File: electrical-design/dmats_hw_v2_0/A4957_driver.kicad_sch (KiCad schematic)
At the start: 21 parts, among them Q1 PSMN1R0-30YLC,115, Q2 PSMN1R0-30YLC,115, Q3 PSMN1R0-30YLC,115, Q4 PSMN1R0-30YLC,115, U1 A4957

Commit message: v2 of circuit for PCB
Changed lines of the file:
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@@
   (symbol (lib_id "Device:R") (at 179.07 99.06 90) (mirror x) (unit 1)
     (in_bom yes) (on_board yes) (dnp no)
-    (property "Reference" "R9" (at 179.07 93.8022 90)
+    (property "Reference" "R9" (at 182.88 95.4786 90)
       (effects (font (size 1.27 1.27)))
     )
-    (property "Value" "1K" (at 179.07 96.1136 90)
+    (property "Value" "1K" (at 182.88 97.79 90)
       (effects (font (size 1.27 1.27)))
     )

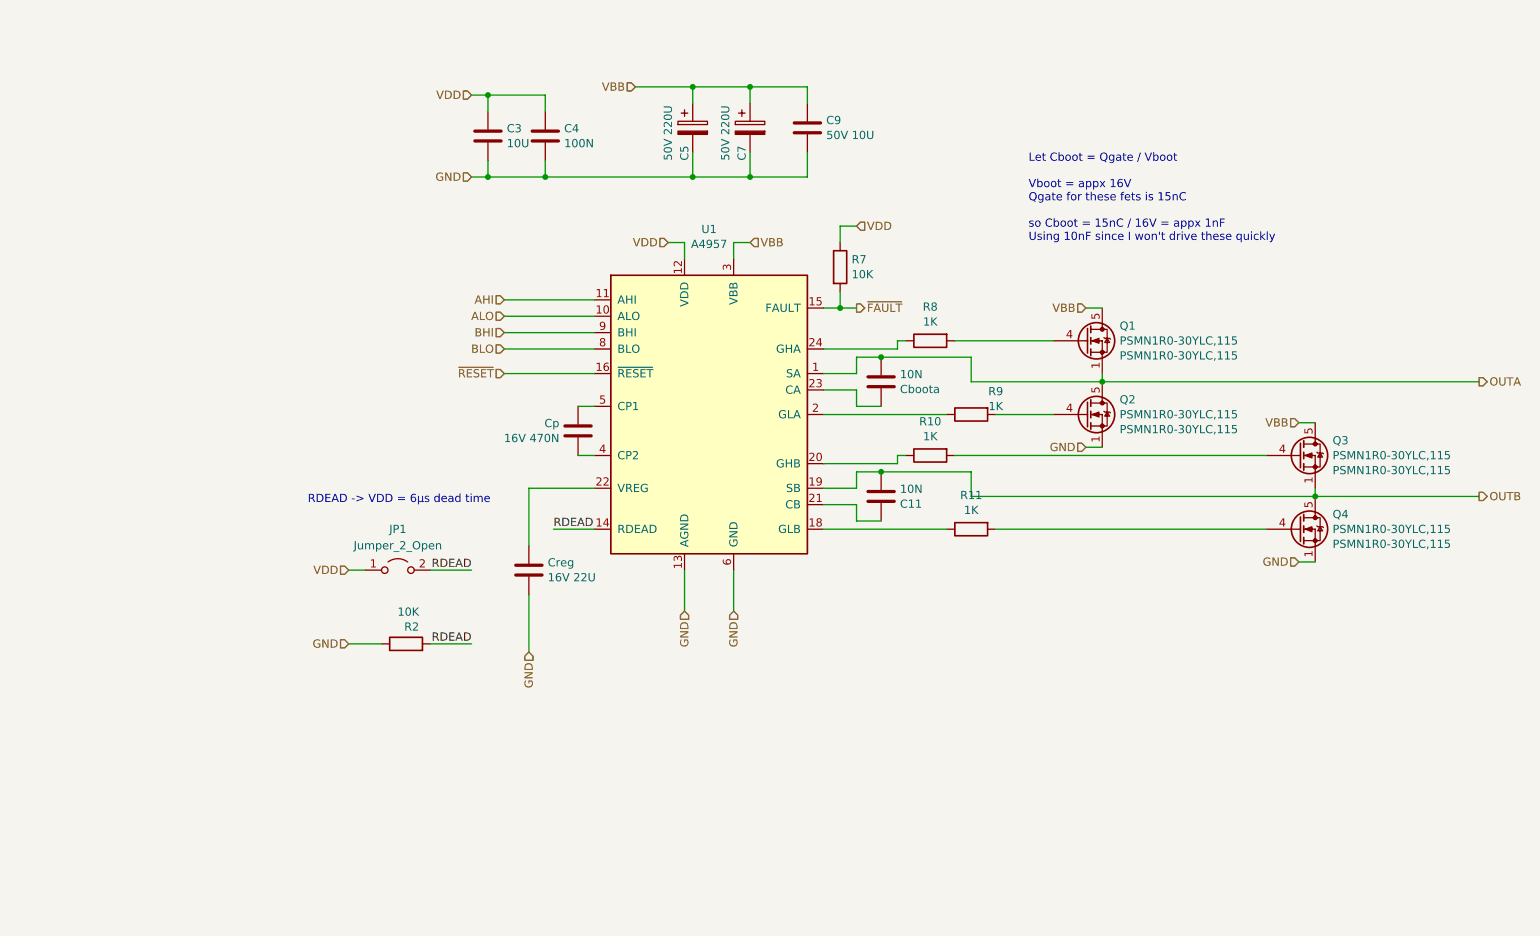
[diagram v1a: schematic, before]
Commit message: created all PCB footprints
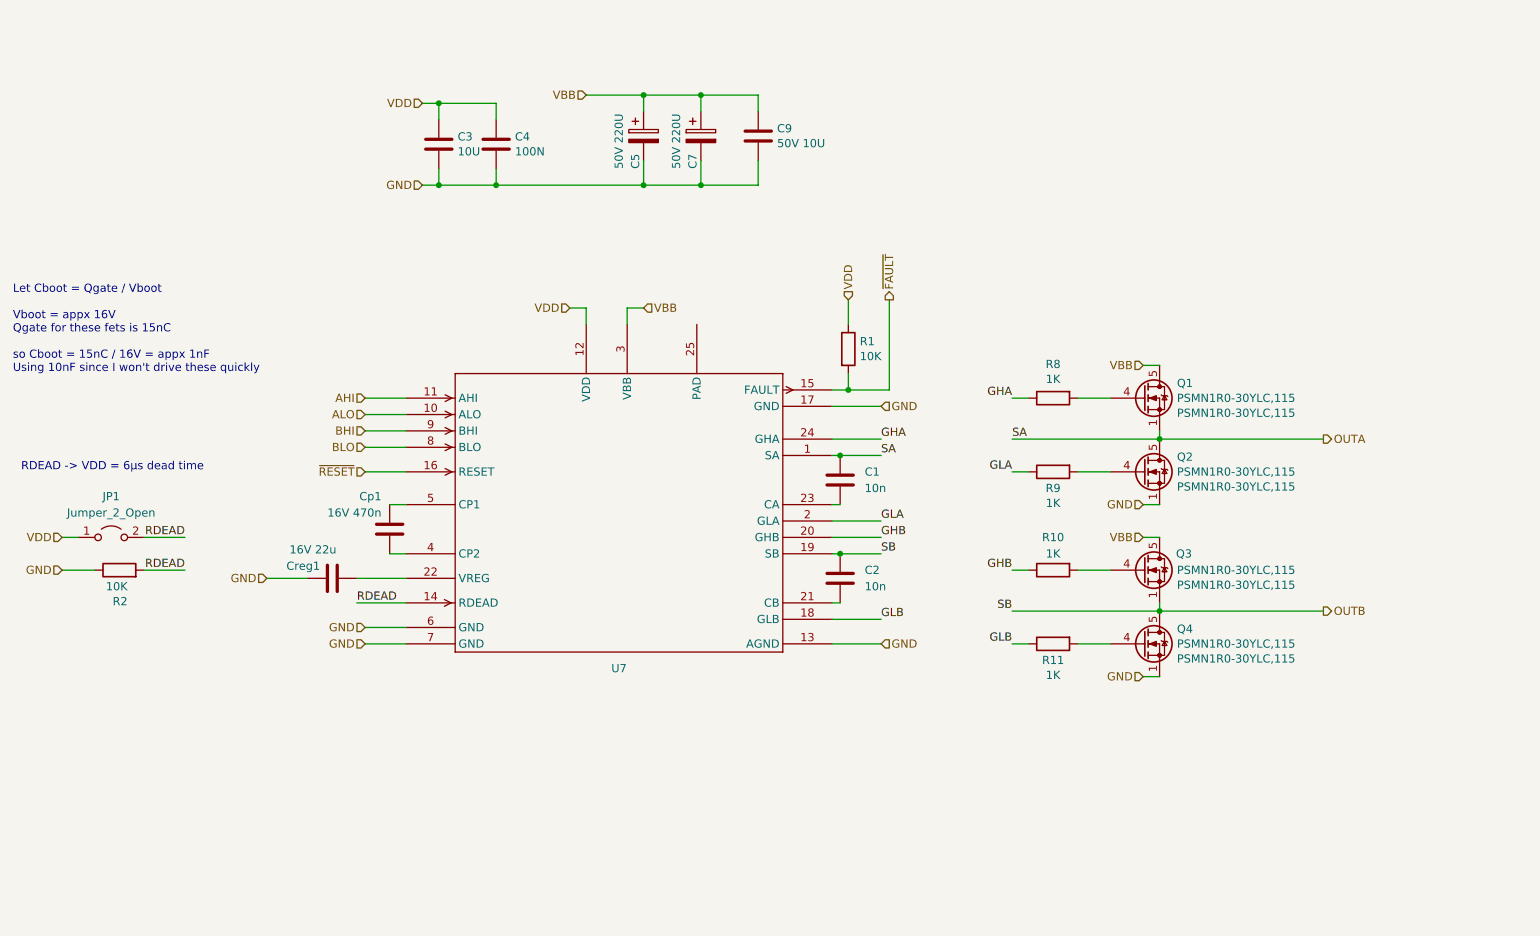
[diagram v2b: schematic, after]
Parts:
- removed C11, Cboota: 10N, Capacitor_SMD:C_0603_1608Metric, symbol Device:C
- removed Cp: 16V 470N, Capacitor_SMD:C_0805_2012Metric, symbol Device:C
- removed Creg: 16V 22U, Capacitor_SMD:C_0805_2012Metric, symbol Device:C
- removed R7: 10K, Resistor_SMD:R_0603_1608Metric, symbol Device:R
- removed U1: A4957, william_motor:A4957, symbol william_motor:A4957
- added C1, C2: 10n, symbol Device:C
- added Cp1: 16V 470n, Capacitor_SMD:C_0805_2012Metric, symbol Device:C
- added Creg1: 16V 22u, Capacitor_SMD:C_0805_2012Metric, symbol Device:C
- added R1: 10K, Resistor_SMD:R_0603_1608Metric, symbol Device:R
- added U7: ~, DMATS_capstone:QFN-24_ALM, symbol DMATS_capstone:A4957
- JP1: footprint (none) -> Resistor_SMD:R_0402_1005Metric_Pad0.72x0.64mm_HandSolder
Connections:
- net AHI: now also U7.11 (AHI)
- net ALO: now also U7.10 (ALO)
- net BHI: now also U7.9 (BHI)
- net BLO: now also U7.8 (BLO)
- net GND: now also Creg1.2, U7.13 (AGND), U7.17 (GND), U7.6 (GND), U7.7 (GND)
- net OUTA: now also C1.1, U7.1 (SA)
- net OUTB: now also C2.1, U7.19 (SB)
- net RDEAD: now also U7.14 (RDEAD)
- net VBB: now also U7.3 (VBB)
- net VDD: now also R1.1, U7.12 (VDD)
- net ~{FAULT}: now also R1.2, U7.15 (FAULT)
- net ~{RESET}: now also U7.16 (RESET)
- net GLA: now reaches R9.1
- net GLA: now also U7.2 (GLA)
- net GHA: now reaches R8.1
- net GHA: now also U7.24 (GHA)
- net GLB: now reaches R11.1
- net GLB: now also U7.18 (GLB)
- net GHB: now reaches R10.1
- net GHB: now also U7.20 (GHB)
- new net: C2.2, U7.21 (CB)
- new net: Cp1.1, U7.4 (CP2)
- new net: Cp1.2, U7.5 (CP1)
- new net: Creg1.1, U7.22 (VREG)
- new net: C1.2, U7.23 (CA)
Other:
- moved on the sheet: C3, C4, C5, C7, C9, JP1, Q1, Q2, Q3, Q4, R10, R11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

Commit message: bulk of PCB design layout complete
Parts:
- C1, C2: footprint (none) -> Capacitor_SMD:C_0603_1608Metric
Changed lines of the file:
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@@
       (effects (font (size 1.27 1.27)) (justify left))
     )
-    (property "Footprint" "" (at 159.7152 128.27 0)
+    (property "Footprint" "Capacitor_SMD:C_0603_1608Metric" (at 159.7152 128.27 0)
       (effects (font (size 1.27 1.27)) hide)
     )
@@
       (effects (font (size 1.27 1.27)) (justify left))
     )
-    (property "Footprint" "" (at 159.7152 113.03 0)
+    (property "Footprint" "Capacitor_SMD:C_0603_1608Metric" (at 159.7152 113.03 0)
       (effects (font (size 1.27 1.27)) hide)
     )

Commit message: PCB work
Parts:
- JP1: footprint Resistor_SMD:R_0402_1005Metric_Pad0.72x0.64mm_HandSolder -> Resistor_SMD:R_0603_1608Metric
- U7: footprint DMATS_capstone:QFN-24_ALM -> Package_DFN_QFN:HVQFN-24-1EP_4x4mm_P0.5mm_EP2.6x2.6mm_ThermalVias
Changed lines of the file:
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@@
       (effects (font (size 1.27 1.27)))
     )
-    (property "Footprint" "Resistor_SMD:R_0402_1005Metric_Pad0.72x0.64mm_HandSolder" (at 45.72 118.11 0)
+    (property "Footprint" "Resistor_SMD:R_0603_1608Metric" (at 45.72 118.11 0)
       (effects (font (size 1.27 1.27)) hide)
     )
@@
       (effects (font (size 1.27 1.27)))
     )
-    (property "Footprint" "DMATS_capstone:QFN-24_ALM" (at 99.06 132.715 0)
+    (property "Footprint" "Package_DFN_QFN:HVQFN-24-1EP_4x4mm_P0.5mm_EP2.6x2.6mm_ThermalVias" (at 99.06 132.715 0)
       (effects (font (size 1.27 1.27)) hide)
     )

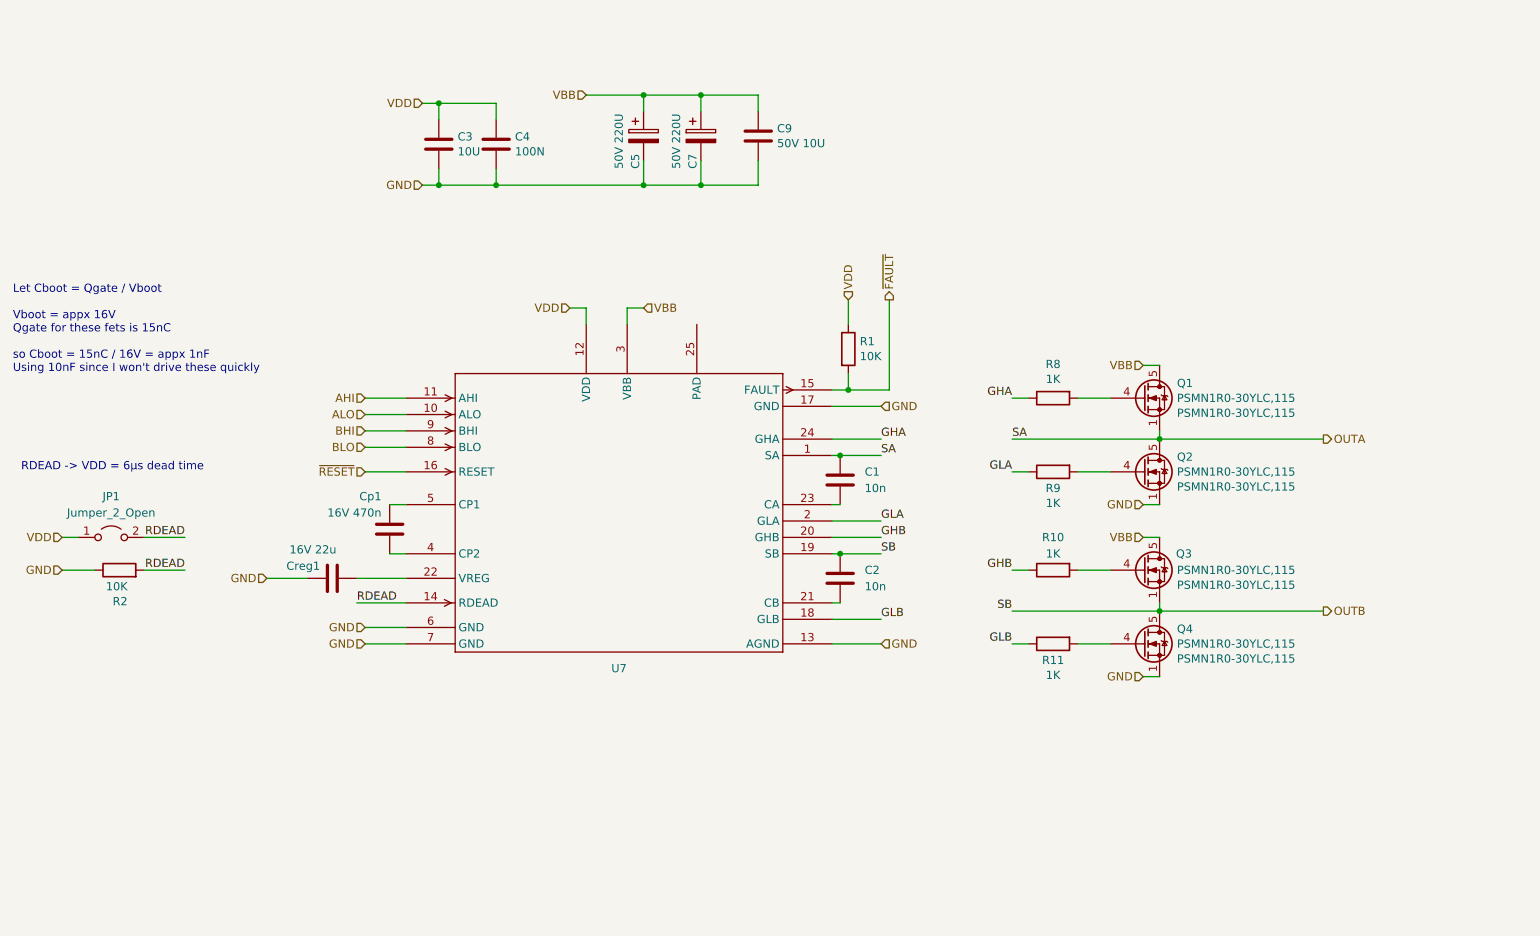
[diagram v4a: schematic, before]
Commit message: sim updates for force analysis and visual clean up on elec drawings
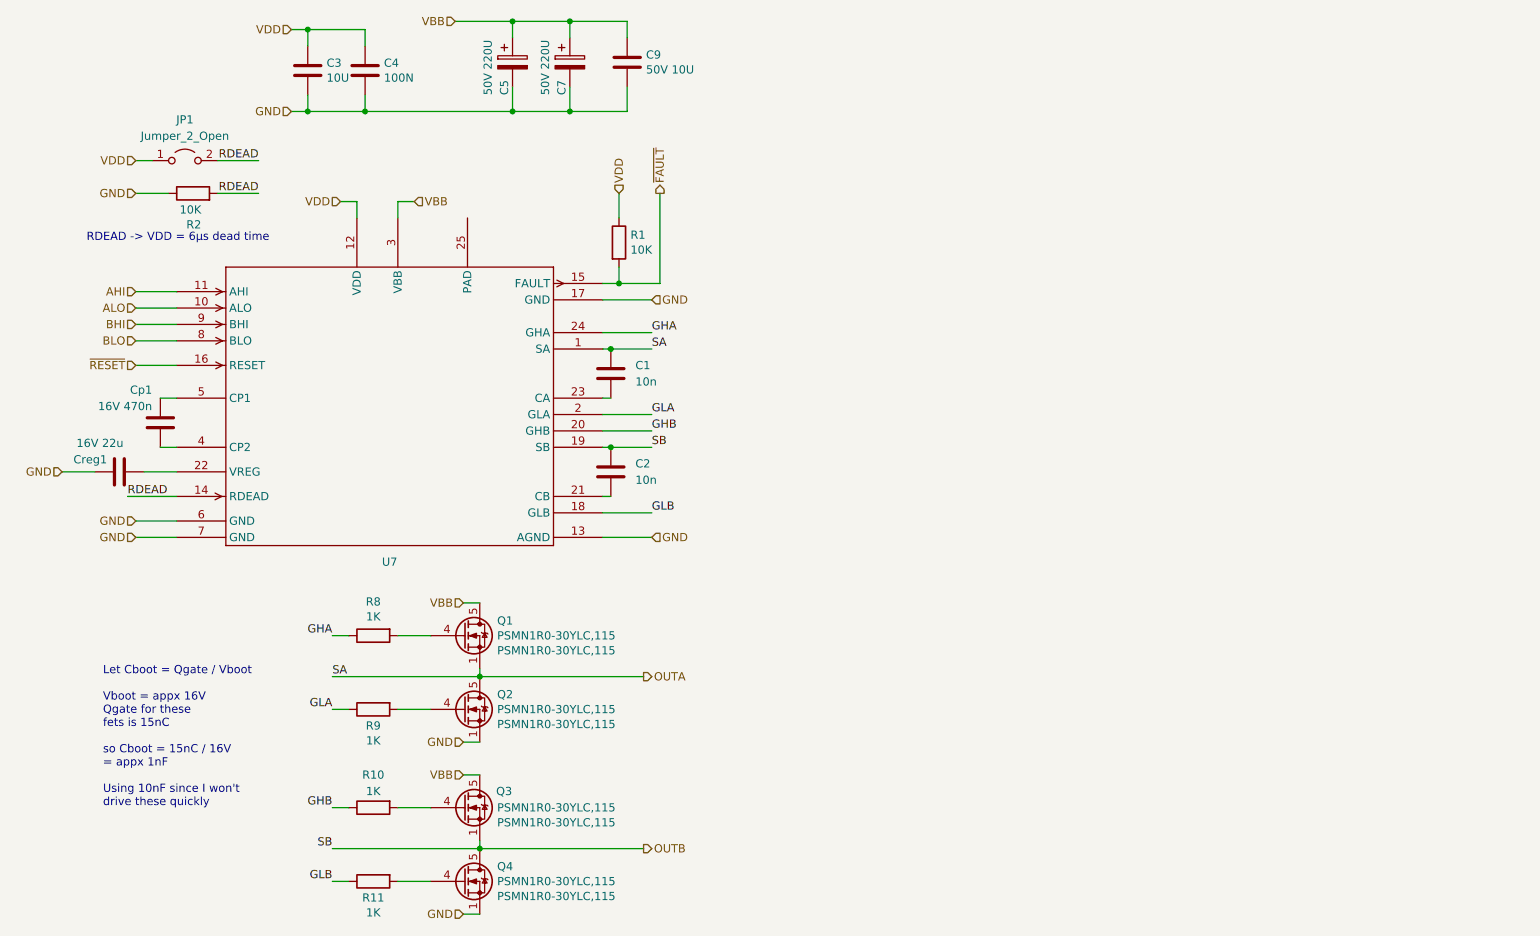
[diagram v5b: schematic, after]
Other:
- moved on the sheet: C1, C2, C3, C4, C5, C7, C9, Cp1, Creg1, JP1, Q1, Q2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
